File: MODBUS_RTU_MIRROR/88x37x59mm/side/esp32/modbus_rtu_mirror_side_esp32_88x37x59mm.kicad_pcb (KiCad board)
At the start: 2 copper layers, 52 x 40 mm, 39 parts, among them J1 Conn_01x04_Male, J2 Conn_01x04_Male, J3 Conn_01x06_Male, SW1 SW_Push, U1 ESP32-WROOM-32, U2 TXS0108EPW, U3 AMS1117-3.3, U4 DS3231MZ, U5 FM24C64C

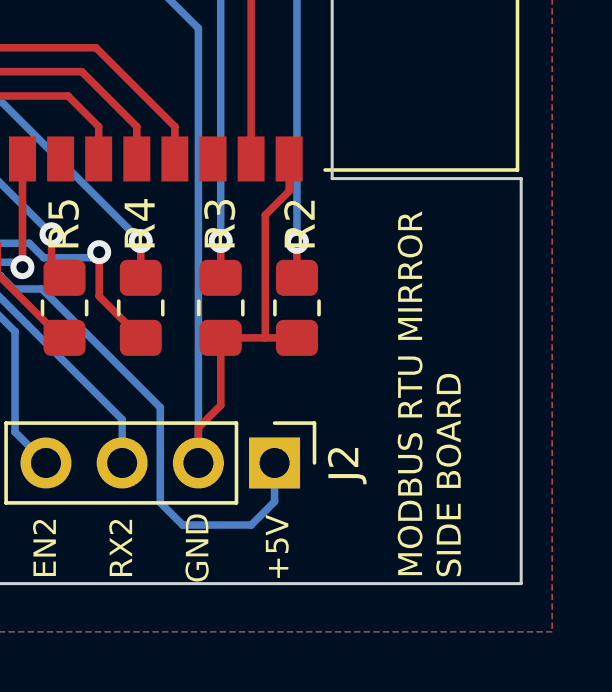
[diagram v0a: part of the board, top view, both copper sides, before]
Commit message: updated pcb silk
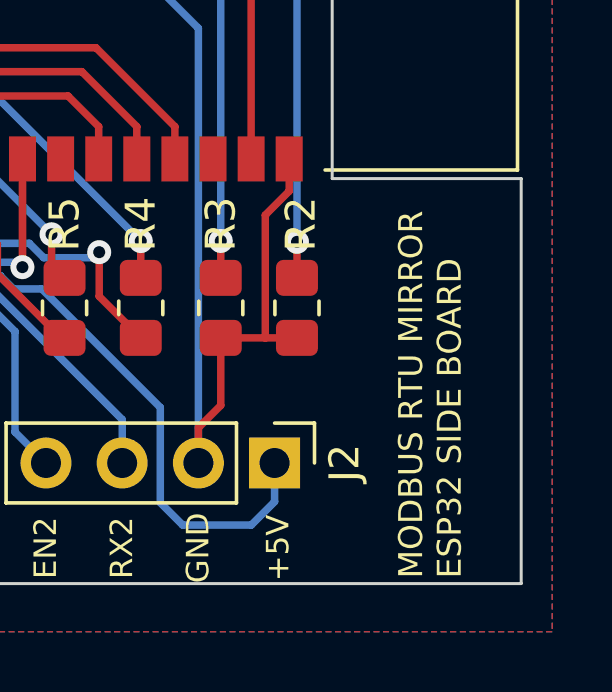
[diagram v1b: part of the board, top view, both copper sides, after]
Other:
- board text added: "MODBUS RTU MIRROR ESP32 SIDE BOARD"
- board text removed: "MODBUS RTU MIRROR SIDE BOARD"
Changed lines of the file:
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@@
     (effects (font (size 0.75 0.75) (thickness 0.1875)) (justify mirror))
   )
-  (gr_text "MODBUS RTU MIRROR\nSIDE BOARD" (at 146.685 101.727) (layer "B.SilkS")
+  (gr_text "MODBUS RTU MIRROR\nESP32 SIDE BOARD" (at 146.685 101.727) (layer "B.SilkS")
     (effects (font (size 0.8 0.8) (thickness 0.2)) (justify left mirror))
   )
@@
     (effects (font (size 0.75 0.75) (thickness 0.1875)))
   )
-  (gr_text "MODBUS RTU MIRROR\nSIDE BOARD" (at 148.971 139.827 90) (layer "F.SilkS")
+  (gr_text "MODBUS RTU MIRROR\nESP32 SIDE BOARD" (at 148.971 139.827 90) (layer "F.SilkS")
     (effects (font (size 0.8 0.8) (thickness 0.2)) (justify left))
   )

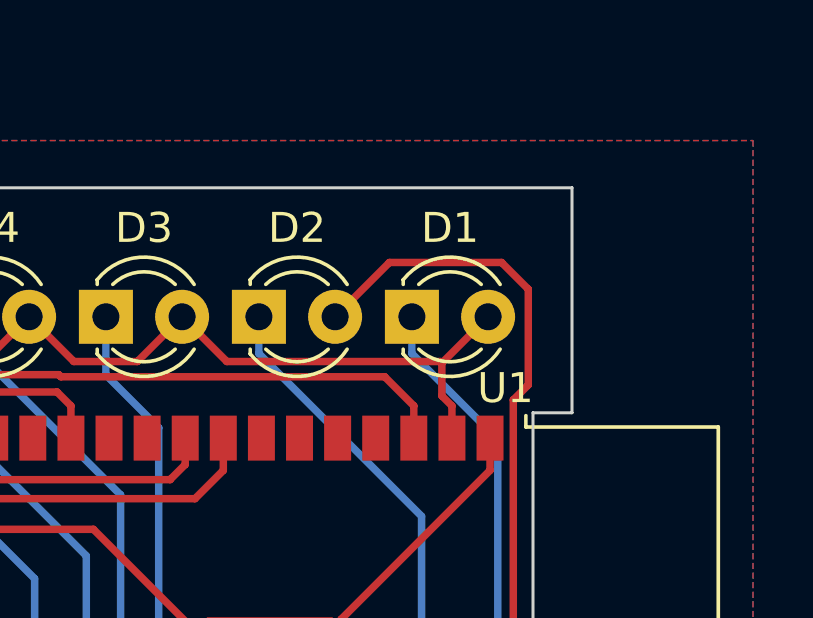
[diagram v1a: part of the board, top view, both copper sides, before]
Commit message: created 90 degree 3mm led socket holder
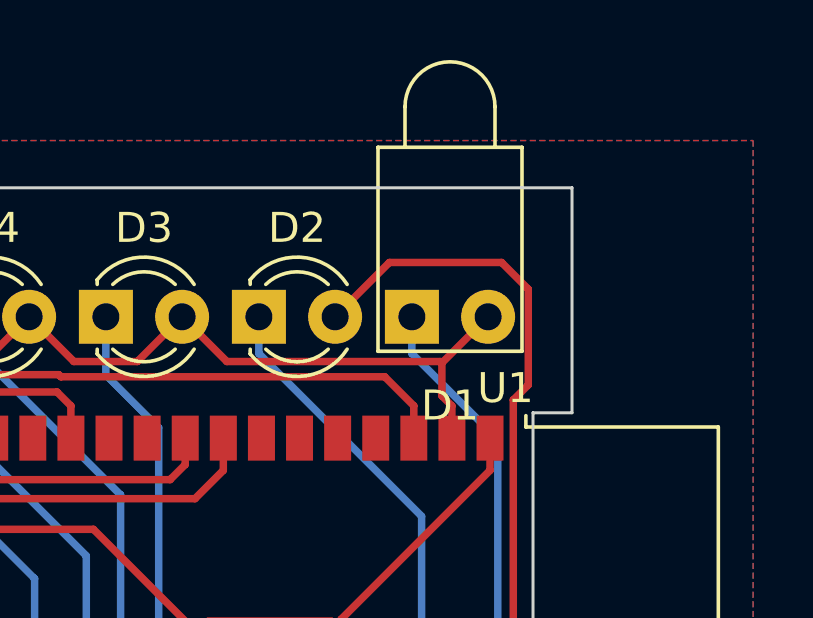
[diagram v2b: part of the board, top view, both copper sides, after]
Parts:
- D1: footprint LED_THT:LED_D3.0mm -> LED_THT_horizontal_holder:LED_D3.0mm_4.5x9.5mm
- turned D1 to 180 degrees

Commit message: changed leds to horizontal and fixed TX1/RX1 disable/enable resistor
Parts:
- D2, D3, D4, D5, D6: footprint LED_THT:LED_D3.0mm -> LED_THT_horizontal_holder:LED_D3.0mm_4.5x9.5mm
- moved D1 1.50 mm to (141.7, 105.8)
- moved D2 1.50 mm to (136.6, 105.8), turned to 180 degrees
- moved D3 1.50 mm to (131.5, 105.8), turned to 180 degrees
- moved D4 1.50 mm to (126.4, 105.8), turned to 180 degrees
- moved D5 1.50 mm to (121.3, 105.8), turned to 180 degrees
- moved D6 1.50 mm to (116.2, 105.8), turned to 180 degrees
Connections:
- J1 pad 3: Net-(J1-Pad3) -> Net-(R10-Pad1)
- J2 pad 4: Net-(J2-Pad4) -> Net-(U2-Pad18)
- R10 pad 1: Net-(J2-Pad4) -> Net-(R10-Pad1)
- R9 pad 1: Net-(J2-Pad4) -> Net-(R10-Pad1)
- U2 pad 15: Net-(J1-Pad3) -> Net-(R10-Pad2)
- U2 pad 18: Net-(R10-Pad2) -> Net-(U2-Pad18)
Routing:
- net Net-(J2-Pad4): track 46.2 -> 0.00 mm, vias 1 -> 0
- net Net-(U2-Pad18): track 0.00 -> 37.3 mm, vias 0 -> 1
- net Net-(R10-Pad1): track 0.00 -> 10.9 mm
- net Net-(J1-Pad3): track 10.5 -> 0.00 mm, vias 1 -> 0
- net +3.3V: track 159.0 -> 165.8 mm
- net Net-(R10-Pad2): track 28.1 -> 21.6 mm, vias 0 -> 2
- net /STP_LED: track 31.1 -> 35.9 mm, vias 0 -> 1
- net /ESP_EN: track 61.7 -> 64.2 mm, vias 0 -> 2
- net Net-(D5-Pad1): track 34.6 -> 33.0 mm
- net Net-(D3-Pad1): track 28.8 -> 27.3 mm
- net Net-(D4-Pad1): track 29.8 -> 28.3 mm
- net Net-(D2-Pad1): track 27.8 -> 26.4 mm
- net Net-(D1-Pad1): track 26.7 -> 25.5 mm
- net Net-(D6-Pad1): track 40.9 -> 39.9 mm
- net /STP_SW: track 32.4 -> 33.1 mm, vias 0 -> 2
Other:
- board text added: "RX1 ONLY INPUT R9 = CLOSE R10 = OPEN"
- board text added: "TX1/RX1 HALF DUP R9 = OPEN R10 = CLOSE"
- board text removed: "RX2 ONLY INPUT R9 = CLOSE R10 = OPEN"
- board text removed: "TX2/RX2 HALF DUP R9 = OPEN R10 = CLOSE"

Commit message: minor modiffications
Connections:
- U1 pad 16: unconnected-(U1-Pad16) -> Net-(U1-Pad16)
- U1 pad 36: unconnected-(U1-Pad36) -> Net-(U1-Pad36)
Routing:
- net GND: track 195.2 -> 194.0 mm
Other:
- board text added: "MODBUS RTU MIRROR ESP32 SIDE BOARD V2"
- board text removed: "MODBUS RTU MIRROR ESP32 SIDE BOARD"

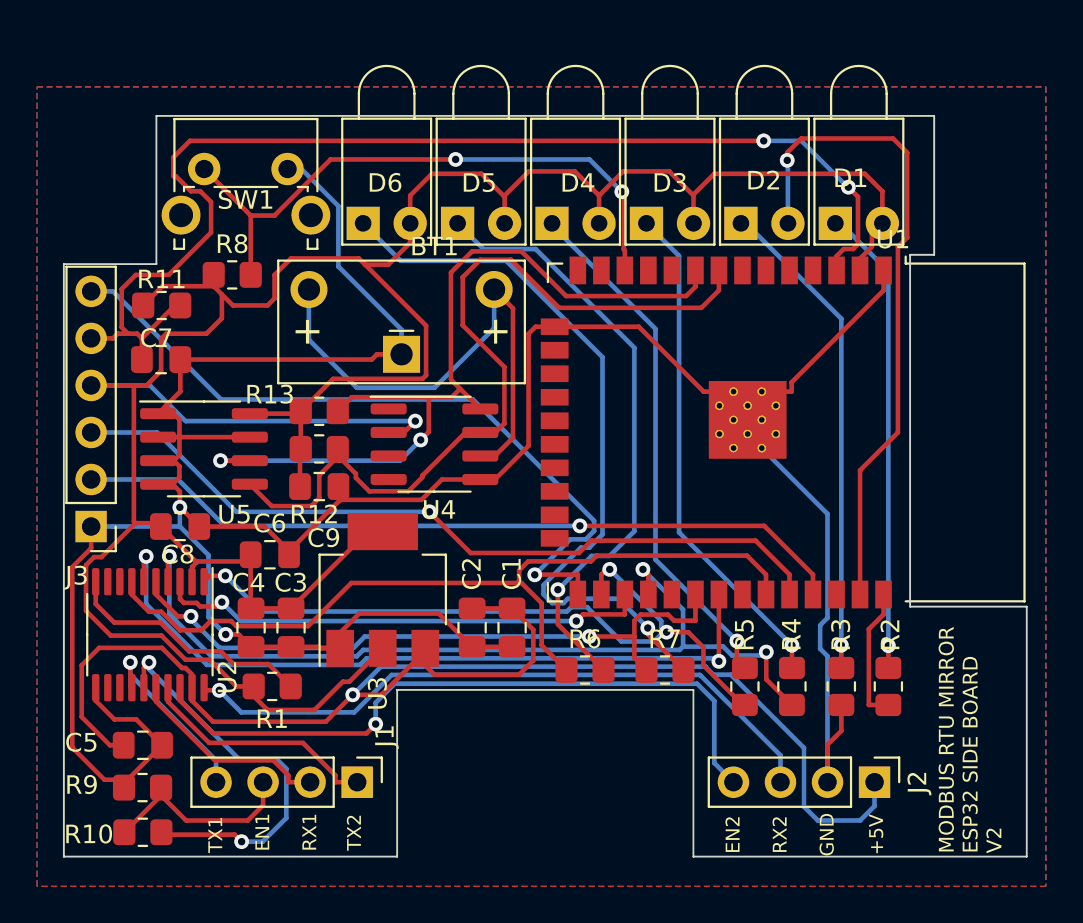
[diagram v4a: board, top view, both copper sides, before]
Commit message: started new branch test, with expansion header
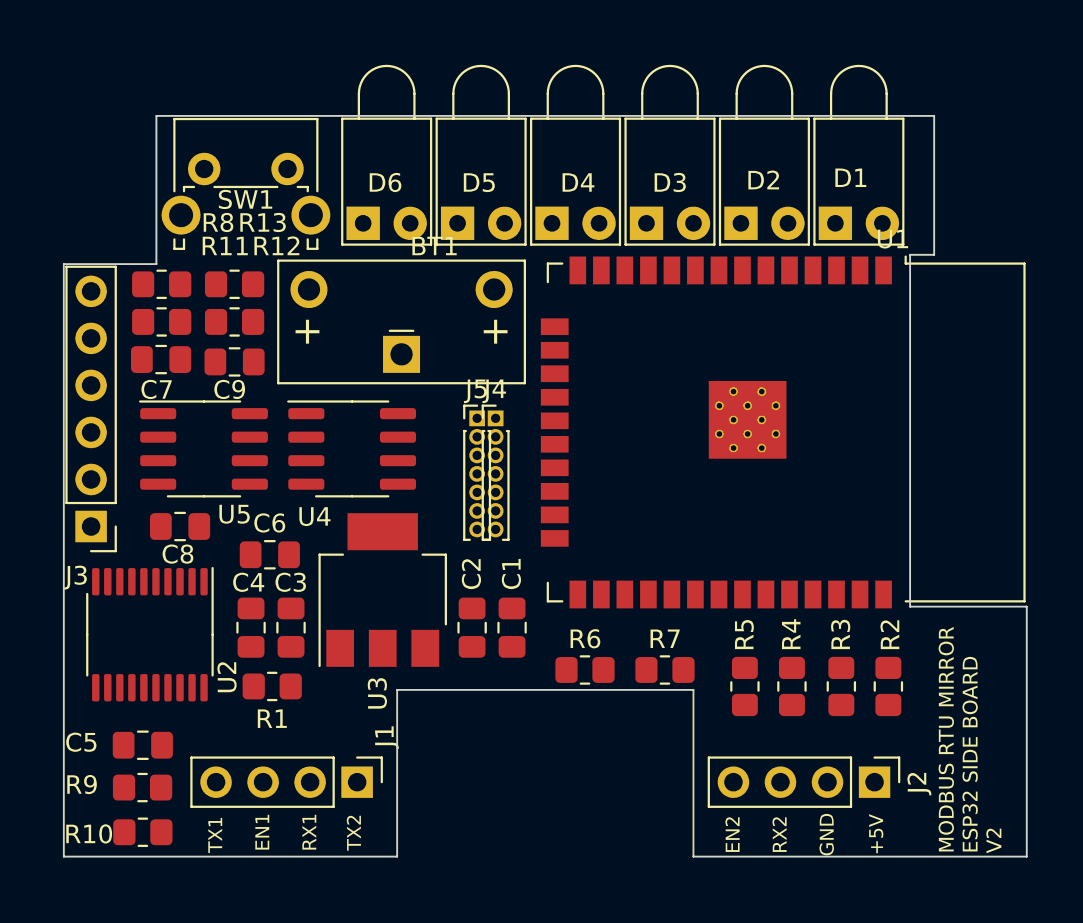
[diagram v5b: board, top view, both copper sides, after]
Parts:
- added J4: Conn_01x07_Male, Connector_PinHeader_1.00mm:PinHeader_1x07_P1.00mm_Vertical, F.Cu at (123.3, 116.3)
- added J5: Conn_01x07_Male, Connector_PinHeader_1.00mm:PinHeader_1x07_P1.00mm_Vertical, F.Cu at (122.3, 116.3)
- moved R12 8.24 mm to (109.2, 111.1)
- moved R13 8.24 mm to (109.2, 109.1)
- moved C9 8.14 mm to (109.2, 113.3)
- moved U4 4.45 mm to (115.6, 118.0)
- moved R8 3.84 mm to (105.3, 109.1)
- moved R11 0.89 mm to (105.3, 111.1)
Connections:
- U1 pad 12: /STP_SW -> /ESP_IO27
- U1 pad 14: unconnected-(U1-Pad14) -> /STP_LED
- U1 pad 16: Net-(U1-Pad16) -> unconnected-(U1-Pad16)
- U1 pad 36: Net-(U1-Pad36) -> unconnected-(U1-Pad36)
- U1 pad 37: /STP_LED -> /ESP_IO23
- U1 pad 4: unconnected-(U1-Pad4) -> /ESP_IO36
- U1 pad 5: unconnected-(U1-Pad5) -> /ESP_IO39
- U1 pad 6: unconnected-(U1-Pad6) -> /ESP_IO34
- U1 pad 7: unconnected-(U1-Pad7) -> /STP_SW
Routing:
- net GND: track 194.0 -> 0.00 mm, vias 2 -> 0
- net +3.3V: track 165.8 -> 0.00 mm, vias 1 -> 0
- net +5V: track 77.3 -> 0.00 mm, vias 1 -> 0
- net /ESP_EN: track 64.2 -> 0.00 mm, vias 2 -> 0
- net /TX2_LED: track 48.2 -> 0.00 mm, vias 3 -> 0
- net /I2C0_SCL: track 46.2 -> 0.00 mm, vias 2 -> 0
- net /TX1_LED: track 45.5 -> 0.00 mm
- net /I2C0_SDA: track 44.6 -> 0.00 mm
- net /ESP_RXD: track 42.5 -> 0.00 mm, vias 1 -> 0
- net /ESP_TXD: track 42.2 -> 0.00 mm, vias 1 -> 0
- net /ESP_IO0: track 40.4 -> 0.00 mm, vias 1 -> 0
- net Net-(U1-Pad31): track 40.1 -> 0.00 mm, vias 2 -> 0
- net Net-(D6-Pad1): track 39.9 -> 0.00 mm, vias 1 -> 0
- net /RX2_LED: track 39.7 -> 0.00 mm, vias 3 -> 0
- net Net-(J2-Pad4): track 37.3 -> 0.00 mm, vias 1 -> 0
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- removed copper zone on B.Cu, net GND
- removed copper zone on F.Cu, net GND

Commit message: expansion connector routed
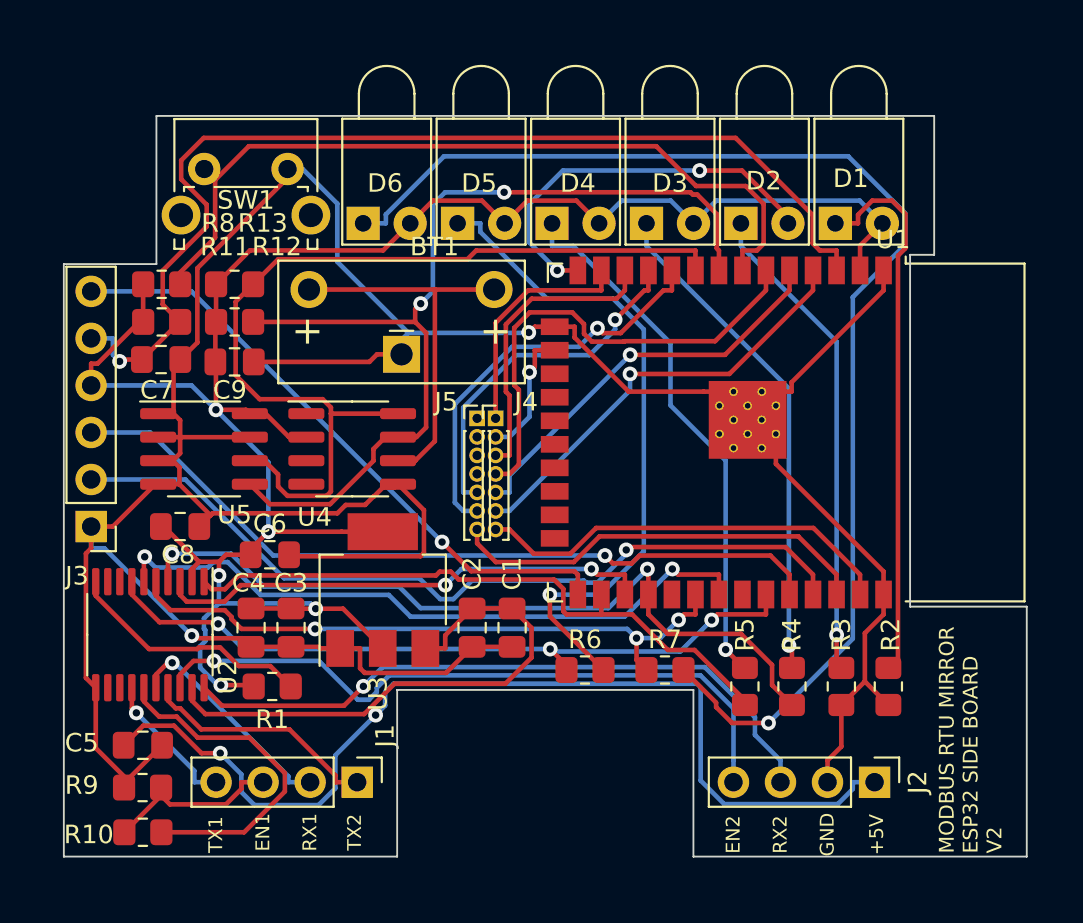
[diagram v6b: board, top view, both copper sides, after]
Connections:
- J4 pad 1: /ESP_IO27 -> /ESP_IO14
- J4 pad 2: /ESP_IO34 -> /ESP_IO13
- J4 pad 3: /ESP_IO39 -> /ESP_IO27
- J4 pad 4: /ESP_IO36 -> /ESP_IO34
- J4 pad 5: /ESP_IO23 -> /ESP_IO39
- J4 pad 6: unconnected-(J4-Pad6) -> /ESP_IO36
- J4 pad 7: unconnected-(J4-Pad7) -> /ESP_IO23
- J5 pad 5: unconnected-(J5-Pad5) -> /ESP_IO26
- J5 pad 6: unconnected-(J5-Pad6) -> /ESP_IO25
- J5 pad 7: unconnected-(J5-Pad7) -> /ESP_IO22
- U1 pad 10: unconnected-(U1-Pad10) -> /ESP_IO25
- U1 pad 11: unconnected-(U1-Pad11) -> /ESP_IO26
- U1 pad 13: unconnected-(U1-Pad13) -> /ESP_IO14
- U1 pad 16: unconnected-(U1-Pad16) -> /ESP_IO13
- U1 pad 36: unconnected-(U1-Pad36) -> /ESP_IO22
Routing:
- net GND: track 0.00 -> 192.2 mm, vias 0 -> 2
- net +3.3V: track 0.00 -> 116.4 mm, vias 0 -> 5
- net +5V: track 0.00 -> 84.0 mm, vias 0 -> 2
- net Net-(D6-Pad1): track 0.00 -> 68.8 mm, vias 0 -> 1
- net /ESP_EN: track 0.00 -> 57.8 mm, vias 0 -> 1
- net /I2C0_SDA: track 0.00 -> 52.7 mm, vias 0 -> 2
- net /I2C0_SCL: track 0.00 -> 50.7 mm
- net /ESP_TXD: track 0.00 -> 44.7 mm, vias 0 -> 1
- net /STP_SW: track 0.00 -> 43.4 mm
- net /ESP_RXD: track 0.00 -> 42.3 mm, vias 0 -> 1
- net /TX2_LED: track 0.00 -> 42.2 mm, vias 0 -> 2
- net /TX1_LED: track 0.00 -> 39.6 mm, vias 0 -> 3
- net Net-(J2-Pad4): track 0.00 -> 37.2 mm, vias 0 -> 1
- net Net-(U1-Pad31): track 0.00 -> 36.2 mm, vias 0 -> 2
- net Net-(J2-Pad3): track 0.00 -> 36.2 mm, vias 0 -> 1
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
